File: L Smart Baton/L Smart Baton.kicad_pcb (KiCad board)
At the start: 2 copper layers, 25 x 200 mm, 51 parts, among them J1 USB4105-GF-A, SW1 B3U-1000P, SW1_R1 1k, U1 MDBT50Q-1MV2, U2 LSM6DSOX, U3 BQ24074RGT, U4 TPS63001

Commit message: Add files via upload
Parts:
- added REF**: MountingHole_2.1mm, MountingHole:MountingHole_2.1mm, F.Cu at (210.0, 148.5)
- added REF**: MountingHole_2.1mm, MountingHole:MountingHole_2.1mm, F.Cu at (218.6, 178.4)
- added REF**: MountingHole_2.1mm, MountingHole:MountingHole_2.1mm, F.Cu at (201.4, 178.4)
- moved R3 251.0 mm to (218.5, 186.0)
- moved RGB_GREEN_R1 233.4 mm to (199.5, 185.3), turned to 90 degrees
- moved R4 231.1 mm to (209.0, 179.3), turned to 90 degrees
- moved RGB_RED_R1 230.0 mm to (203.5, 185.3), turned to 90 degrees
- moved D1 228.8 mm to (218.5, 188.0)
- moved R2 223.5 mm to (214.7, 136.4), turned to -90 degrees
- moved R5 221.6 mm to (212.2, 180.1)
- moved RGB_BLUE_R1 220.0 mm to (201.5, 185.3), turned to 90 degrees
- moved R1 203.2 mm to (213.2, 136.4), turned to 90 degrees
- moved R_CHG_PULLUP1 200.4 mm to (211.5, 177.5), turned to 90 degrees
- moved +3V3 198.4 mm to (220.0, 163.0)
- moved J_SWD1 196.9 mm to (220.0, 135.4)
- moved LED_RGB1 195.0 mm to (201.0, 188.0), turned to 180 degrees
- moved GND1 193.6 mm to (220.0, 165.5)
- moved VBUS1 193.3 mm to (220.0, 168.0)
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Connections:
- U1 pad 22: unconnected-(U1-P0.06-Pad22) -> /BLE_LED
- U1 pad 43: /BLE_LED -> (no net)
- U1 pad 46: /RGB_RED -> (no net)
- U1 pad 47: unconnected-(U1-P1.00-Pad47) -> /RGB_RED
- U1 pad 48: /RGB_BLUE -> (no net)
- U1 pad 49: unconnected-(U1-P0.25-Pad49) -> /RGB_BLUE
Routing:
- net +3V3: track 0.00 -> 174.9 mm, vias 0 -> 13
- net GND: track 0.00 -> 123.4 mm, vias 0 -> 20
- net /RGB_GREEN: track 0.00 -> 69.6 mm, vias 0 -> 2
- net /BLE_LED: track 0.00 -> 68.1 mm, vias 0 -> 4
- net /RGB_BLUE: track 0.00 -> 66.8 mm, vias 0 -> 2
- net /RGB_RED: track 0.00 -> 66.5 mm, vias 0 -> 2
- net /CHG_STATUS: track 0.00 -> 62.0 mm, vias 0 -> 4
- net Net-(J_BAT1-Pin_1): track 0.00 -> 61.4 mm, vias 0 -> 2
- net /SW_POW: track 0.00 -> 52.7 mm, vias 0 -> 4
- net Net-(U1-P0.26): track 0.00 -> 45.1 mm
- net Net-(POWER_SWITCH1-A): track 0.00 -> 40.5 mm
- net Net-(U3-IN): track 0.00 -> 35.7 mm, vias 0 -> 6
- net Net-(U1-P0.27): track 0.00 -> 30.2 mm, vias 0 -> 2
- net /SWDCLK: track 0.00 -> 27.1 mm, vias 0 -> 1
- net /SWDIO: track 0.00 -> 26.4 mm, vias 0 -> 1
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- added copper zone on B.Cu, net GND
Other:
- board size 25 x 200 mm -> 23 x 83 mm
- rule pad_to_mask_clearance: 0 -> 0.0762

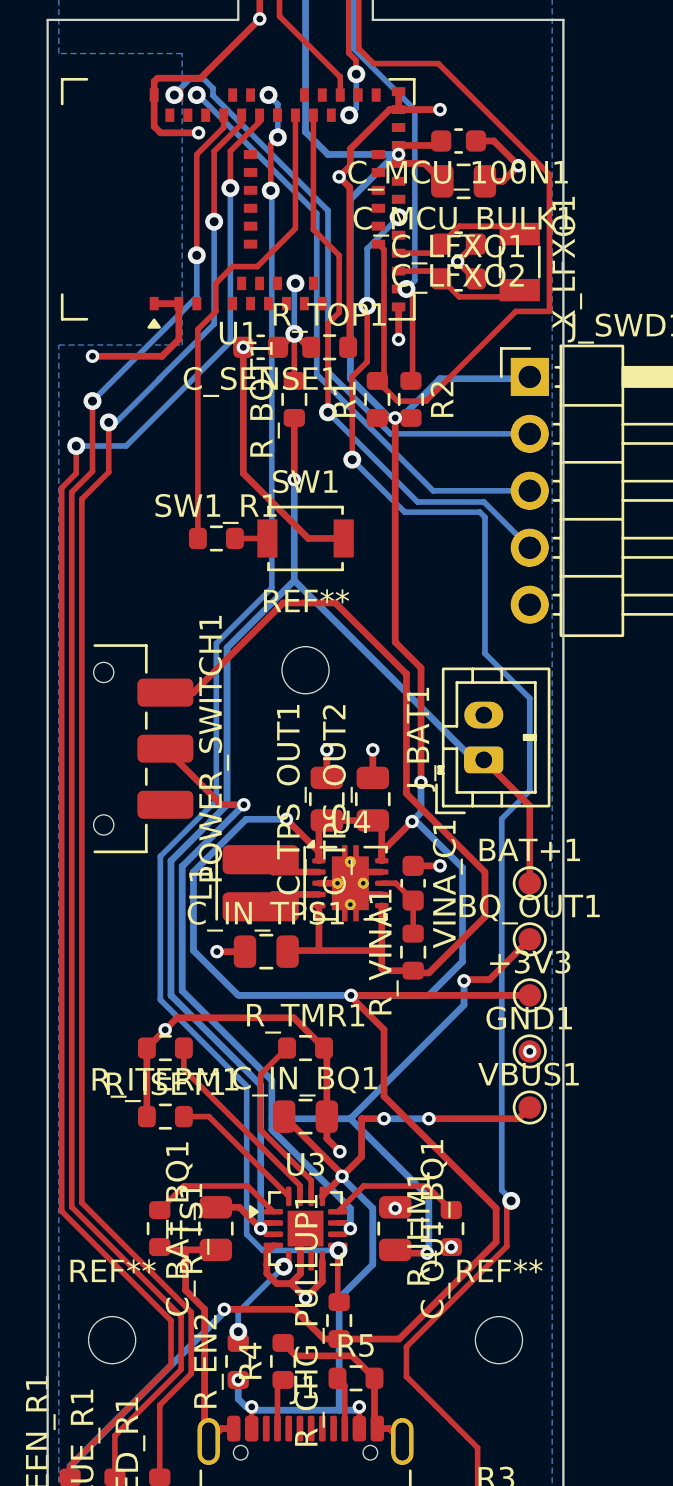
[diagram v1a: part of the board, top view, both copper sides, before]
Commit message: Draft before via movements due to violations
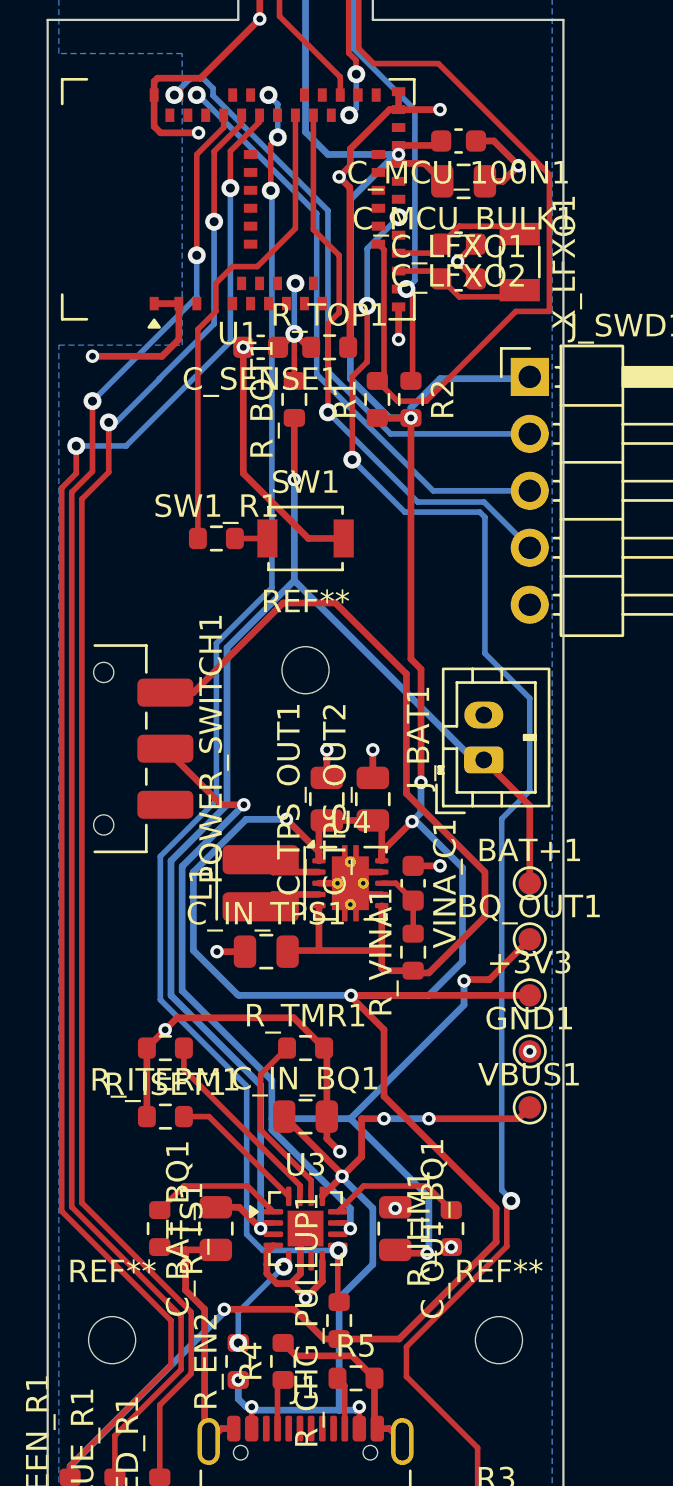
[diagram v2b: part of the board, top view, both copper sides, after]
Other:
- rule pad_to_mask_clearance: 0.0762 -> 0

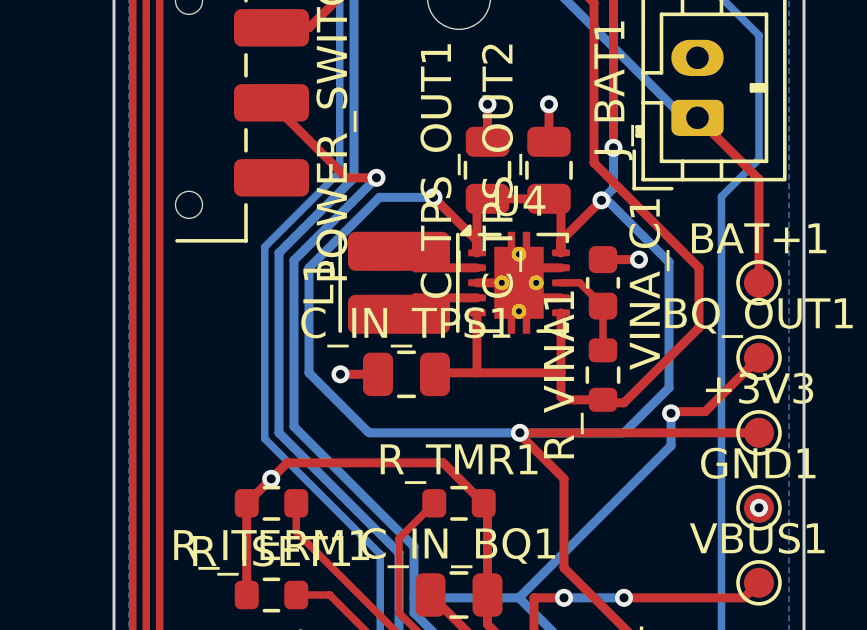
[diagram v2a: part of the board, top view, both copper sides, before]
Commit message: Changed unavailable components with substitute pads. FINAL DRAFT
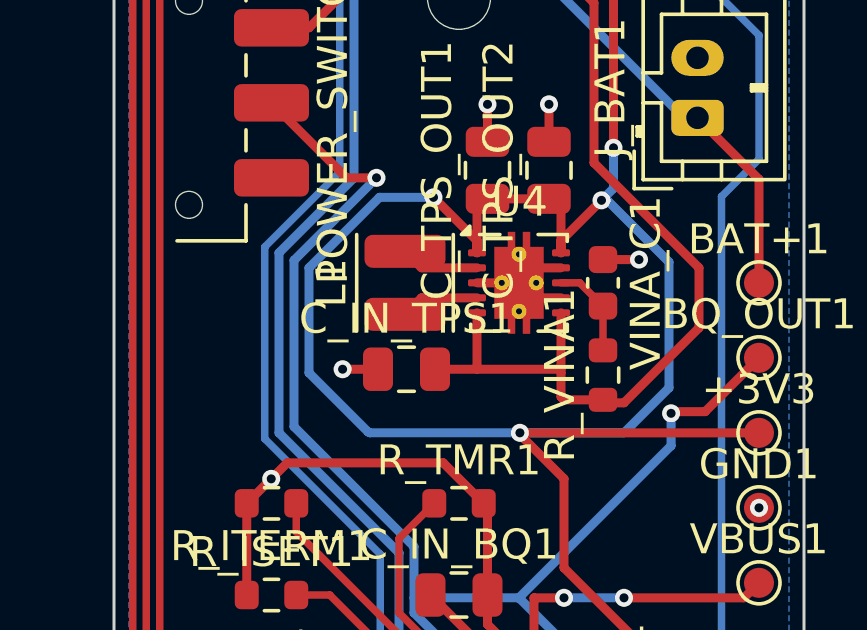
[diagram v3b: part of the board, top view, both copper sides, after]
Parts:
- J1: value USB4105-GF-A -> TYPEC-304A-ACP16W
- L1: value 74438335022 -> MPN3015S2R2MT; footprint Inductor_SMD:L_Wuerth_MAPI-3015 -> Inductor_SMD:L_Sunlord_SWPA3015S
- moved L1 0.20 mm to (208.2, 158.0)
- moved C_IN_TPS1 0.17 mm to (208.2, 160.9)
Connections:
- U1 pad 43: (no net) -> unconnected-(U1-P0.21-Pad43)
- U1 pad 46: (no net) -> unconnected-(U1-P0.22-Pad46)
- U1 pad 48: (no net) -> unconnected-(U1-P0.24-Pad48)
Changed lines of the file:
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@@
 			(size 0.6 0.4)
 			(layers "F.Cu" "F.Mask" "F.Paste")
+			(net "unconnected-(U1-P0.21-Pad43)")
 			(pinfunction "P0.21_43")
-			(pintype "no_connect")
+			(pintype "bidirectional+no_connect")
 		)
 		(pad "44" smd rect
@@
 			(size 0.6 0.4)
 			(layers "F.Cu" "F.Mask" "F.Paste")
+			(net "unconnected-(U1-P0.22-Pad46)")
 			(pinfunction "P0.22_46")
-			(pintype "no_connect")
+			(pintype "bidirectional+no_connect")
 		)
 		(pad "47" smd rect
@@
 			(size 0.6 0.4)
 			(layers "F.Cu" "F.Mask" "F.Paste")
+			(net "unconnected-(U1-P0.24-Pad48)")
 			(pinfunction "P0.24_48")
-			(pintype "no_connect")
+			(pintype "bidirectional+no_connect")
 		)
 		(pad "49" smd rect
@@
 	(footprint "Capacitor_SMD:C_0805_2012Metric"
 		(layer "F.Cu")
-		(at 208.25 161.05)
+		(at 208.25 160.88)
 		(descr "Capacitor SMD 0805 (2012 Metric), square (rectangular) end terminal, IPC-7351 nominal, (Body size source: IPC-SM-782 page 76, https://www.pcb-3d.com/wordpress/wp-content/uploads/ipc-sm-782a_amendment_1_and_2.pdf, https://docs.google.com/spreadsheets/d/1BsfQQcO9C6DZCsRaXUlFlo91Tg2WpOkGARC1WS5S8t0/edit?usp=sharing)")
 		(tags "capacitor")
@@
 		(embedded_fonts no)
 	)
-	(footprint "Inductor_SMD:L_Wuerth_MAPI-3015"
+	(footprint "Inductor_SMD:L_Sunlord_SWPA3015S"
 		(layer "F.Cu")
-		(at 208 158 90)
-		(descr "Inductor, Wuerth, MAPI-3015, 3.0x3.0x1.5mm, (https://www.we-online.com/en/components/products/WE-MAPI?kicad)")
-		(tags "Würth SMT")
+		(at 208.2 158 90)
+		(descr "Inductor, Sunlord, SWPA3015S, 3.0x3.0x1.5mm, (https://www.sunlordinc.com/UploadFiles/PDF_Cat/20120704094224784.pdf)")
+		(tags "swpa")
 		(property "Reference" "L1"
-			(at 0 -2.65 90)
+			(at 0 -2.45 90)
 			(layer "F.SilkS")
 			(effects
@@
 			)
 		)
-		(property "Value" "74438335022"
-			(at 0 2.65 90)
+		(property "Value" "MPN3015S2R2MT"
+			(at 0 2.45 90)
 			(layer "F.Fab")
 			(effects
@@
 			)
 		)
-		(property "Datasheet" "https://www.we-online.com/en/components/products/WE-MAPI?utm_source=chatgpt.com"
+		(property "Datasheet" ""
 			(at 0 0 90)
 			(layer "F.Fab")
@@
 		(duplicate_pad_numbers_are_jumpers no)
 		(fp_line
-			(start -1.61 -1.96)
-			(end 1.61 -1.96)
+			(start -1.61 -1.61)
+			(end 1.61 -1.61)
 			(stroke
 				(width 0.12)
@@
 		)
 		(fp_line
-			(start 1.61 1.96)
-			(end -1.61 1.96)
+			(start 1.61 1.61)
+			(end -1.61 1.61)
 			(stroke
 				(width 0.12)
@@
 		)
 		(fp_line
-			(start 1.95 -1.95)
-			(end 1.95 1.95)
+			(start 1.75 -1.75)
+			(end 1.75 -1.6)
 			(stroke
 				(width 0.05)
@@
 		)
 		(fp_line
-			(start 0.15 -1.95)
-			(end 1.95 -1.95)
+			(start -1.75 -1.75)
+			(end 1.75 -1.75)
 			(stroke
 				(width 0.05)
@@
 		)
 		(fp_line
-			(start -0.15 -1.95)
-			(end -0.15 -1.75)
+			(start 1.8 -1.6)
+			(end 1.8 1.6)
 			(stroke
 				(width 0.05)
@@
 		)
 		(fp_line
-			(start -1.95 -1.95)
-			(end -0.15 -1.95)
+			(start 1.75 -1.6)
+			(end 1.8 -1.6)
 			(stroke
 				(width 0.05)
@@
 		)
 		(fp_line
-			(start 0.15 -1.75)
-			(end 0.15 -1.95)
+			(start -1.75 -1.6)
+			(end -1.75 -1.75)
 			(stroke
 				(width 0.05)
@@
 		)
 		(fp_line
-			(start -0.15 -1.75)
-			(end 0.15 -1.75)
+			(start -1.8 -1.6)
+			(end -1.75 -1.6)
 			(stroke
 				(width 0.05)
@@
 		)
 		(fp_line
-			(start 0.15 1.75)
-			(end -0.15 1.75)
+			(start 1.8 1.6)
+			(end 1.75 1.6)
 			(stroke
 				(width 0.05)
@@
 		)
 		(fp_line
-			(start -0.15 1.75)
-			(end -0.15 1.95)
+			(start 1.75 1.6)
+			(end 1.75 1.75)
 			(stroke
 				(width 0.05)
@@
 		)
 		(fp_line
-			(start 1.95 1.95)
-			(end 0.15 1.95)
+			(start -1.75 1.6)
+			(end -1.8 1.6)
 			(stroke
 				(width 0.05)
@@
 		)
 		(fp_line
-			(start 0.15 1.95)
-			(end 0.15 1.75)
+			(start -1.8 1.6)
+			(end -1.8 -1.6)
 			(stroke
 				(width 0.05)
@@
 		)
 		(fp_line
-			(start -0.15 1.95)
-			(end -1.95 1.95)
+			(start 1.75 1.75)
+			(end -1.75 1.75)
 			(stroke
 				(width 0.05)
@@
 		)
 		(fp_line
-			(start -1.95 1.95)
-			(end -1.95 -1.95)
+			(start -1.75 1.75)
+			(end -1.75 1.6)
 			(stroke
 				(width 0.05)
@@
 		(pad "1" smd roundrect
 			(at -1.05 0 90)
-			(size 1.3 3.4)
+			(size 1.1 2.7)
 			(layers "F.Cu" "F.Mask" "F.Paste")
-			(roundrect_rratio 0.192308)
+			(roundrect_rratio 0.25)
 			(net "Net-(U4-L1)")
 			(pinfunction "1_1")
@@
 		(pad "2" smd roundrect
 			(at 1.05 0 90)
-			(size 1.3 3.4)
+			(size 1.1 2.7)
 			(layers "F.Cu" "F.Mask" "F.Paste")
-			(roundrect_rratio 0.192308)
+			(roundrect_rratio 0.25)
 			(net "Net-(U4-L2)")
 			(pinfunction "2_2")
@@
 		)
 		(embedded_fonts no)
-		(model "${KICAD10_3DMODEL_DIR}/Inductor_SMD.3dshapes/L_Wuerth_MAPI-3015.step"
+		(model "${KICAD10_3DMODEL_DIR}/Inductor_SMD.3dshapes/L_Sunlord_SWPA3015S.step"
 			(offset
 				(xyz 0 0 0)
@@
 			)
 		)
-		(property "Value" "USB4105-GF-A"
+		(property "Value" "TYPEC-304A-ACP16W"
 			(at 0 5 0)
 			(unlocked yes)
@@
 			)
 		)
-		(property "Datasheet" "https://gct.co/files/drawings/usb4105.pdf"
+		(property "Datasheet" ""
 			(at 0 0 0)
 			(unlocked yes)
@@
 	)
 	(segment
-		(start 206.05 161.05)
-		(end 207.3 161.05)
-		(width 0.3)
-		(layer "F.Cu")
-		(net "GND")
-	)
-	(segment
 		(start 210.5 113.935)
 		(end 210.025 113.935)
@@
 	)
 	(segment
+		(start 206.12 160.88)
+		(end 207.3 160.88)
+		(width 0.3)
+		(layer "F.Cu")
+		(net "GND")
+	)
+	(segment
 		(start 216 157.225)
 		(end 214.8 157.225)
@@
 	)
 	(via
-		(at 206.05 161.05)
-		(size 0.6)
-		(drill 0.3)
-		(layers "F.Cu" "B.Cu")
-		(net "GND")
-	)
-	(via
 		(at 213 152.05)
 		(size 0.6)
@@
 	)
 	(via
+		(at 206.12 160.88)
+		(size 0.6)
+		(drill 0.3)
+		(layers "F.Cu" "B.Cu")
+		(net "GND")
+	)
+	(via
 		(at 216 123.5)
 		(size 0.6)
@@
 	)
 	(segment
-		(start 209.25 161)
-		(end 210.6 161)
+		(start 210.6 160.88)
+		(end 210.6 159)
 		(width 0.3)
 		(layer "F.Cu")
@@
 	)
 	(segment
-		(start 213.4 161)
-		(end 210.6 161)
+		(start 209.2 160.88)
+		(end 213.4 160.88)
 		(width 0.3)
 		(layer "F.Cu")
@@
 	)
 	(segment
-		(start 210.6 161)
-		(end 210.6 159)
-		(width 0.3)
-		(layer "F.Cu")
-		(net "Net-(POWER_SWITCH1-A)")
-	)
-	(segment
 		(start 218 159.5)
 		(end 218 157.5)
@@
 	)
 	(segment
-		(start 208.55 157.5)
-		(end 210.6 157.5)
+		(start 208.75 157.5)
+		(end 208.2 156.95)
 		(width 0.3)
 		(layer "F.Cu")
@@
 	)
 	(segment
-		(start 208 156.95)
-		(end 208.55 157.5)
+		(start 210.6 157.5)
+		(end 208.75 157.5)
 		(width 0.3)
 		(layer "F.Cu")
@@
 	)
 	(segment
-		(start 208.55 158.5)
-		(end 210.6 158.5)
+		(start 208.75 158.5)
+		(end 208.2 159.05)
 		(width 0.3)
 		(layer "F.Cu")
@@
 	)
 	(segment
-		(start 208 159.05)
-		(end 208.55 158.5)
+		(start 210.6 158.5)
+		(end 208.75 158.5)
 		(width 0.3)
 		(layer "F.Cu")
